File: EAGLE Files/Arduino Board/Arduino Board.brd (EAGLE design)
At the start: 72.4 x 67.3 mm, 14 parts

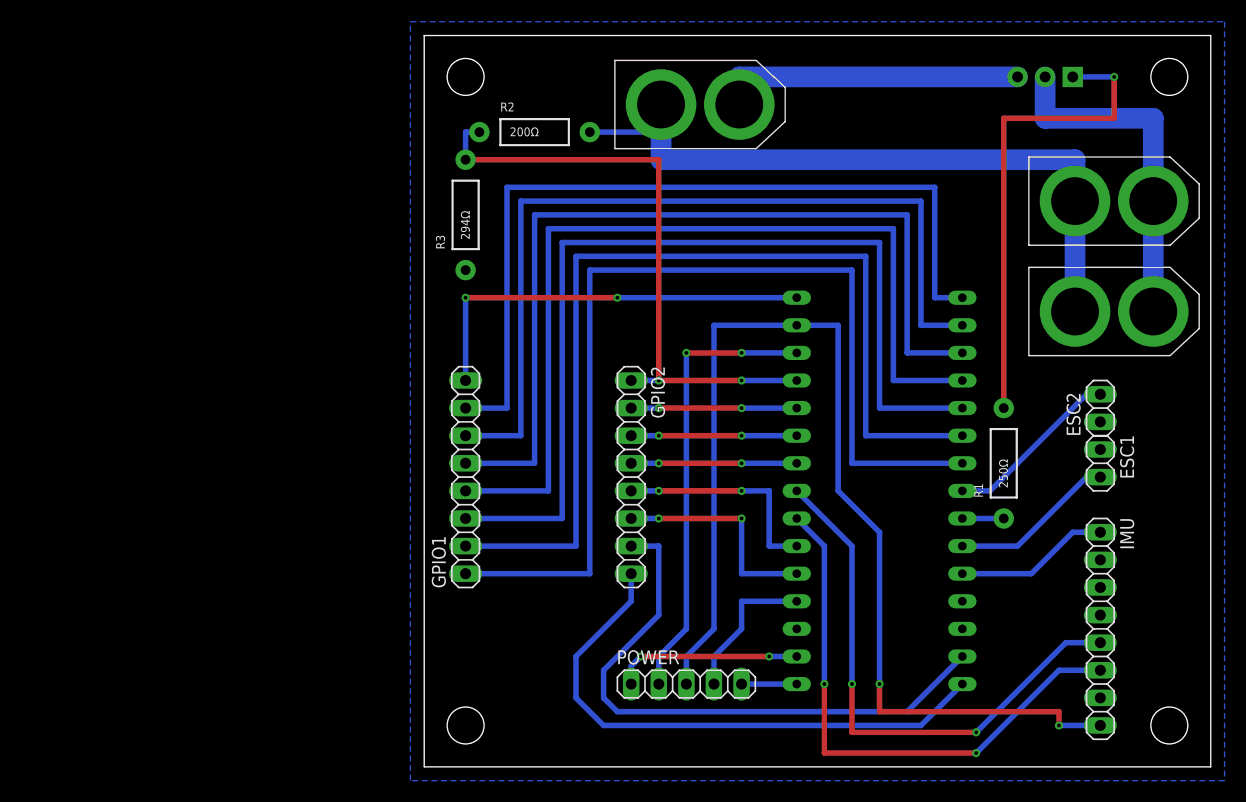
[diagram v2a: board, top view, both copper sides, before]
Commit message: Small changes to PCB design files from EAGLE software update
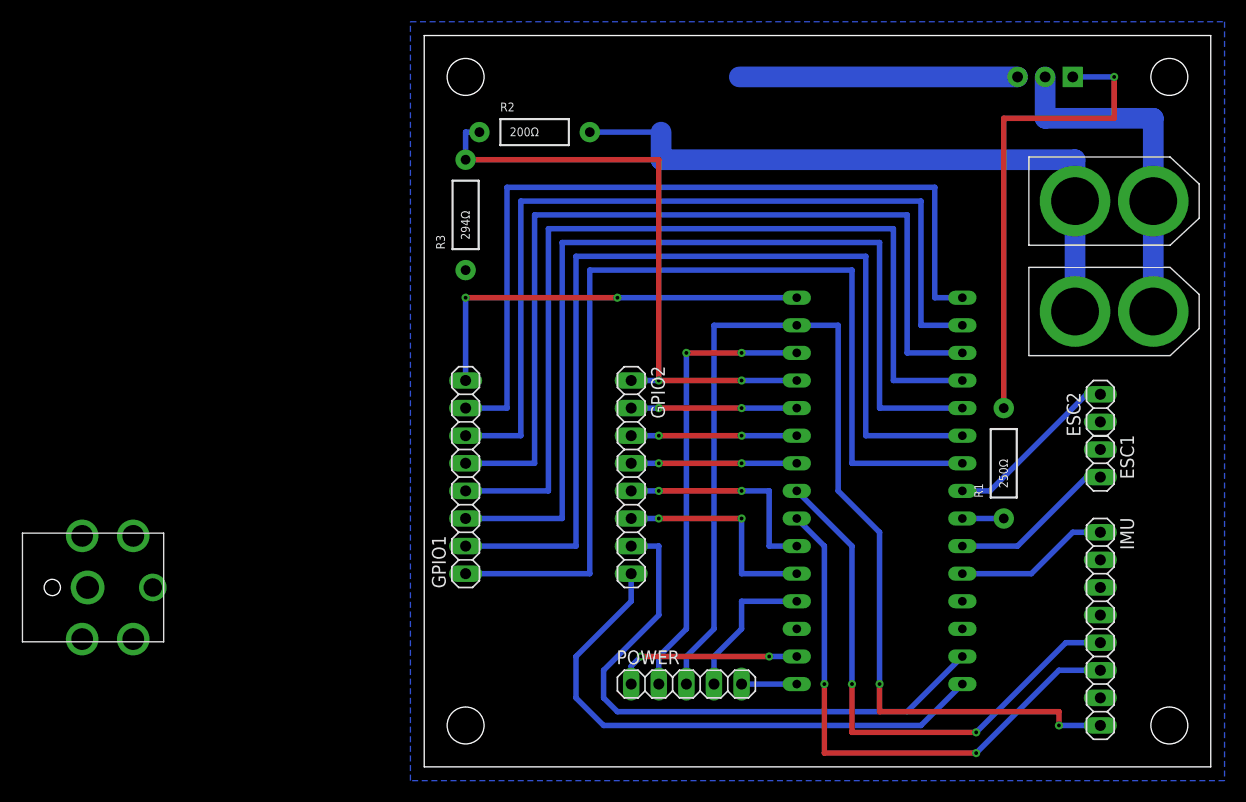
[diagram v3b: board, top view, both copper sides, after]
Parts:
- removed BATTERY_POWER: XT60, Controls Library:XT60
- added POWER_JACK: PJ-082BH, Controls Library:PJ-082BH
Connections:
- net GND: now also POWER_JACK.2, POWER_JACK.SH1, POWER_JACK.SH2, POWER_JACK.SH3, POWER_JACK.SH4; no longer BATTERY_POWER.-
- net SUPPLY+: now also POWER_JACK.1; no longer BATTERY_POWER.+
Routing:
- net SUPPLY+: track 63.7 -> 61.2 mm
- net GND: track 45.4 -> 42.9 mm
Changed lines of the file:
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@@
 <?xml version="1.0" encoding="utf-8"?>
 <!DOCTYPE eagle SYSTEM "eagle.dtd">
-<eagle version="8.4.3">
+<eagle version="8.5.2">
 <drawing>
 <settings>
@@
 <param name="checkRestrict" value="1"/>
 <param name="checkStop" value="0"/>
+<param name="checkValues" value="0"/>
 <param name="useDiameter" value="13"/>
 <param name="maxErrors" value="50"/>
@@
 </autorouter>
 <elements>
-<element name="BATTERY_POWER" library="Controls Library" package="XT60" value="XT60" x="25.4" y="60.96" rot="R270"/>
 <element name="ESC1" library="Controls Library" package="1X02" value="M02" x="62.23" y="27.94" rot="R270"/>
 <element name="ESC1_POWER" library="Controls Library" package="XT60" value="XT60" x="63.5" y="41.91" rot="R270"/>
@@
 <element name="R2" library="Controls Library" package="AXIAL-0.4" value="200Ω" x="10.16" y="58.42"/>
 <element name="R3" library="Controls Library" package="AXIAL-0.4" value="294Ω" x="3.81" y="50.8" rot="R90"/>
+<element name="POWER_JACK" library="Controls Library" package="PJ-082BH" value="PJ-082BH" x="-30.48" y="16.51"/>
 </elements>
 <signals>
@@
 <wire x1="19.05" y1="9.271" x2="19.05" y2="7.62" width="0.508" layer="16"/>
 <contactref element="POWER_MOSFET" pad="3"/>
-<contactref element="BATTERY_POWER" pad="-"/>
-<wire x1="29" y1="60.96" x2="29" y2="63.5" width="1.905" layer="16"/>
 <wire x1="29" y1="63.5" x2="54.61" y2="63.5" width="1.905" layer="16"/>
 <contactref element="R3" pad="P$1"/>
+<contactref element="POWER_JACK" pad="2"/>
+<contactref element="POWER_JACK" pad="SH2"/>
+<contactref element="POWER_JACK" pad="SH1"/>
+<contactref element="POWER_JACK" pad="SH4"/>
+<contactref element="POWER_JACK" pad="SH3"/>
+<wire x1="62.23" y1="29.21" x2="62.23" y2="31.75" width="0" layer="19" extent="1-1"/>
+<wire x1="49.53" y1="15.24" x2="62.23" y2="29.21" width="0" layer="19" extent="1-1"/>
+<wire x1="62.23" y1="6.35" x2="49.53" y2="15.24" width="0" layer="19" extent="1-1"/>
+<wire x1="34.29" y1="10.16" x2="49.53" y2="15.24" width="0" layer="19" extent="1-1"/>
+<wire x1="54.61" y1="63.5" x2="62.23" y2="31.75" width="0" layer="19" extent="1-1"/>
+<wire x1="3.81" y1="45.72" x2="29" y2="63.5" width="0" layer="19" extent="16-16"/>
+<wire x1="-26.78" y1="21.26" x2="3.81" y2="45.72" width="0" layer="19" extent="1-1"/>
+<wire x1="-31.48" y1="21.26" x2="-26.78" y2="21.26" width="0" layer="19" extent="1-1"/>
+<wire x1="-30.98" y1="16.51" x2="-31.48" y2="21.26" width="0" layer="19" extent="1-1"/>
+<wire x1="-31.48" y1="11.76" x2="-30.98" y2="16.51" width="0" layer="19" extent="1-1"/>
+<wire x1="-26.78" y1="11.76" x2="-31.48" y2="11.76" width="0" layer="19" extent="1-1"/>
 </signal>
 <signal name="INT">
@@
 </signal>
 <signal name="SUPPLY+">
-<contactref element="BATTERY_POWER" pad="+"/>
 <contactref element="ESC1_POWER" pad="+"/>
 <contactref element="ESC2_POWER" pad="+"/>
@@
 <wire x1="21.8" y1="58.42" x2="21.8" y2="55.88" width="1.905" layer="16"/>
 <contactref element="R2" pad="P$2"/>
-<wire x1="21.8" y1="58.42" x2="21.8" y2="60.96" width="1.905" layer="16"/>
 <wire x1="15.24" y1="58.42" x2="21.8" y2="58.42" width="0.508" layer="16"/>
+<contactref element="POWER_JACK" pad="1"/>
+<wire x1="-24.98" y1="16.51" x2="15.24" y2="58.42" width="0" layer="19" extent="1-1"/>
 </signal>
 <signal name="SUPPLY-">
